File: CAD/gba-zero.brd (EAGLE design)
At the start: 15.2 x 11.4 mm, 20 parts, among them IC5 APX803, Q2 BSS138

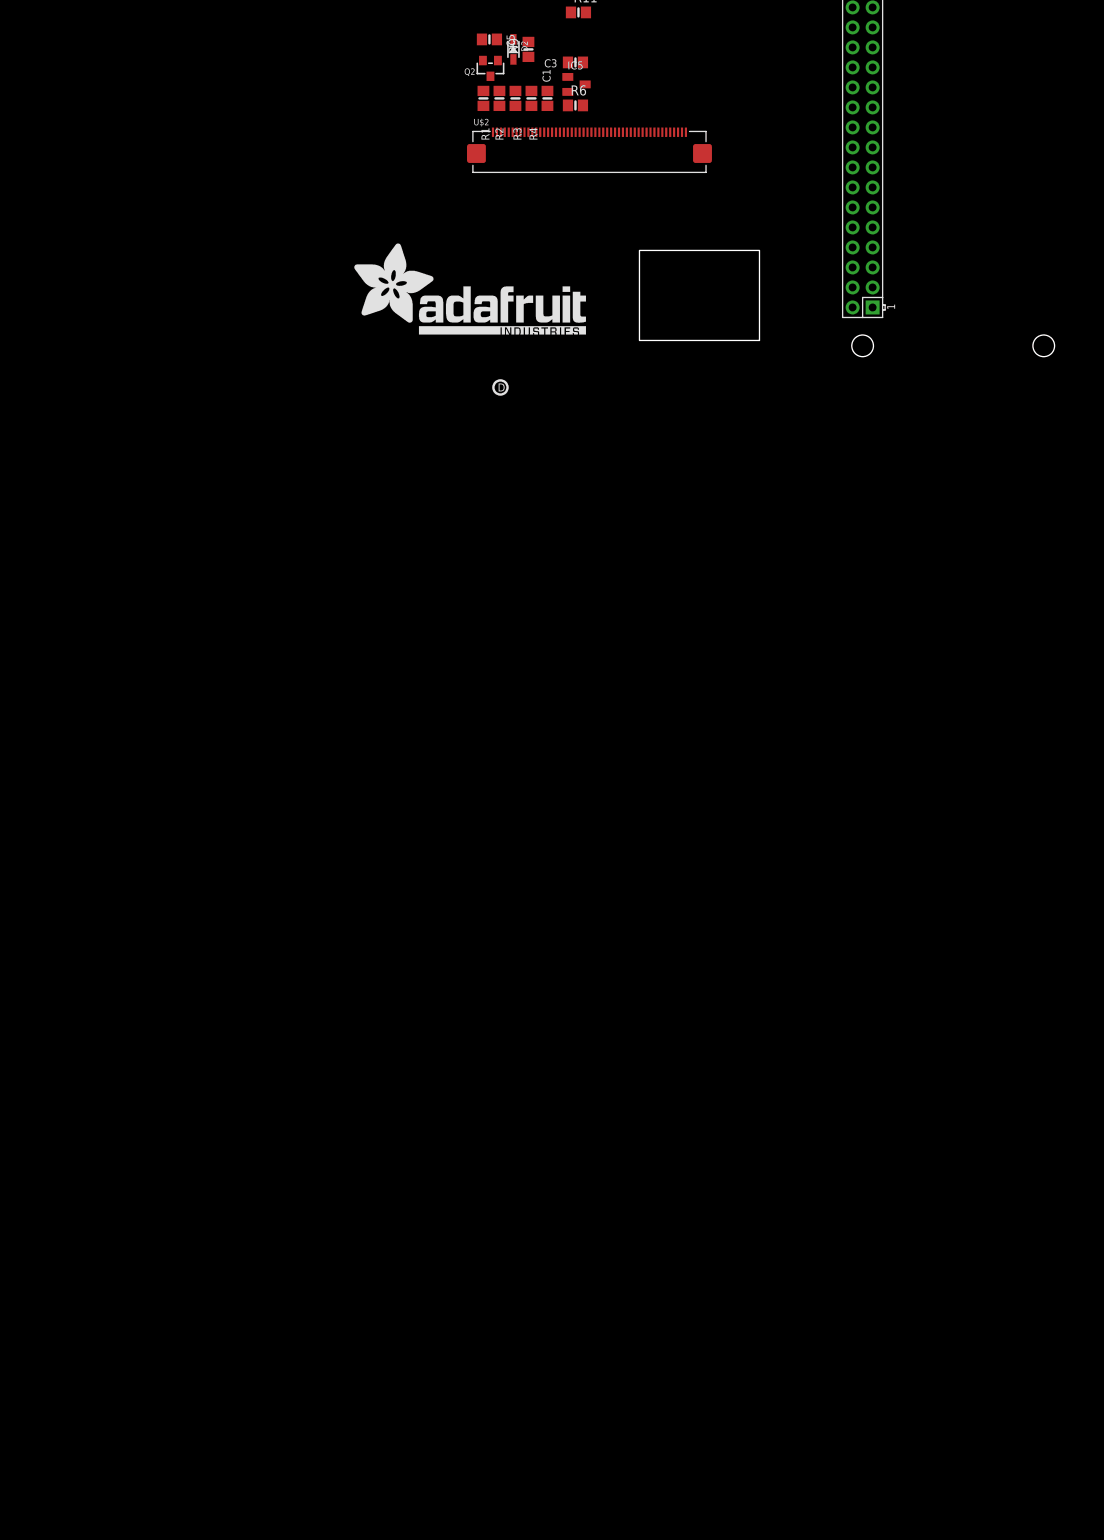
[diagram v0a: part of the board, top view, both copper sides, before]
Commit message: Parts & Schematic almost done, except AB buttons
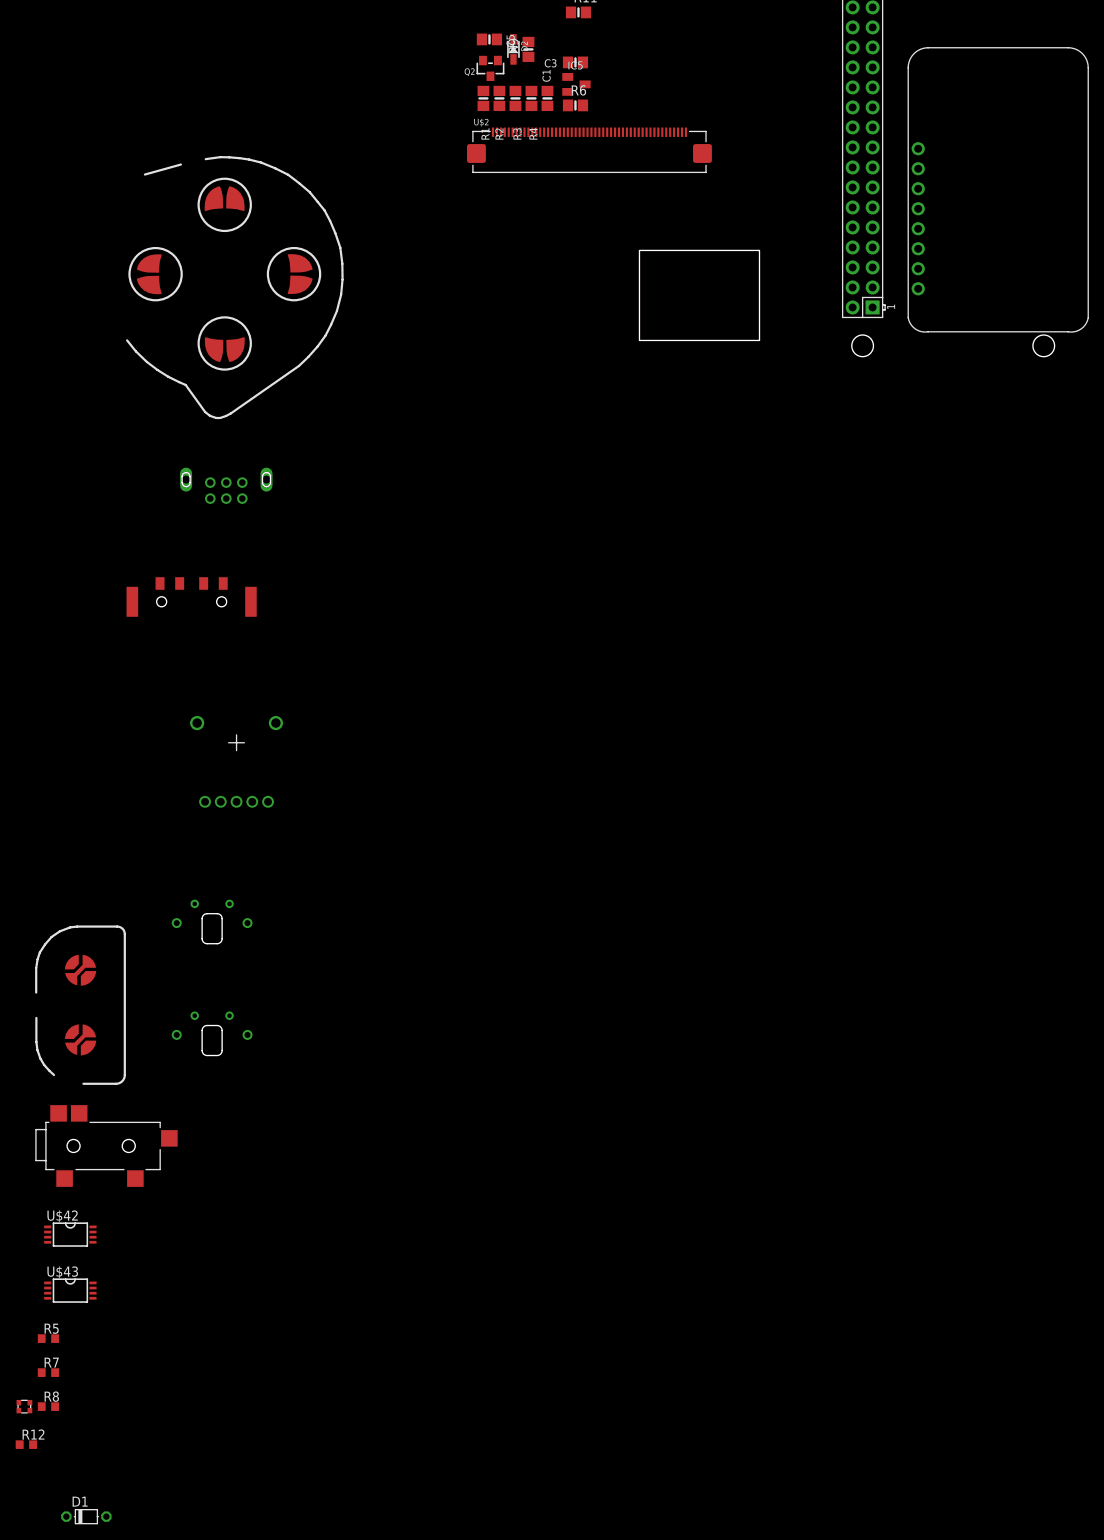
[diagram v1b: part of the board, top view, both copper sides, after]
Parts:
- removed U$23: (no value), microbuilder:ADAFRUIT_TEXT_20MM
- added D1: (no value), diode:D-5
- added R12: 10KΩ, resistor:R0603
- added R5, R7: 250Ω, resistor:R0603
- added R8: 167Ω, resistor:R0603
- added U$10: LINK_CONNECTOR, gba-zero-parts:LINK_CONNECTOR
- added U$11: PWR_SWITCH, gba-zero-parts:PWR-SWITCH
- added U$15: RK10J12E0A0A, gba-zero-parts:RK10J12E0A0A
- added U$16, U$17: SHOULDER_BUTTON, gba-zero-parts:SHOULDER_BUTTON
- added U$18: START_SELECT_BUTTON, gba-zero-parts:START_SELECT_BUTTON
- added U$22: SWTCHCRFT_3.5JACK5-JACK-SMD, gba-zero-parts:4-JACK-SMD
- added U$3: D-PAD, gba-zero-parts:D-PAD
- added U$43: 74LVC3G04, gba-zero-parts:TSSOP-8
- added U$44: LTST-C19HE1WT, gba-zero-parts:WL-SBCW-0606
- U$12: value (none) -> POWERBOOST-1000C; device microbuilder:PCBFEAT-REV-040 -> gba-zero-parts:POWERBOOST-1000C
- U$2: value DISP_LCD_240X320_50PIN_2.8IN -> (none); device microbuilder:TFT_2.83IN_240X320_50PIN -> gba-zero-parts:TFT_2.83IN_240X320_50PIN
- U$42: value (none) -> 74LVC2G02; device microbuilder:ADAFRUIT_TEXT_30MM -> gba-zero-parts:TSSOP-8
- moved U$42 119.8 mm to (-34.8, -105.2)
- moved U$12 67.4 mm to (71.6, 45.5), turned to 270 degrees
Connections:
- new net GPIO17: U$17.BIG-1, U$17.SMALL-1, U$7.11
- new net GPIO19: U$18.SEL, U$7.35
- new net GPIO20: U$11.L, U$7.38
- new net GPIO21: D1.A, U$7.40
- new net GPIO22: U$3.RIGHT, U$7.15
- new net GPIO26: U$18.STR, U$7.37
- new net GPIO27: U$3.LEFT, U$7.13
- new net GPIO4: U$16.BIG-1, U$16.SMALL-1, U$7.7
- new net GPIO5: U$3.UP, U$7.29
- new net GPIO6: U$3.DOWN, U$7.31
- new net LBO: U$12.LBO, U$42.6
- new net N$11: R8.1, U$43.2
- new net N$12: R5.2, U$44.B
- new net N$13: R7.2, U$44.G
- new net N$14: R8.2, U$44.R
- new net N$15: U$42.7, U$43.1
- new net N$16: U$42.1, U$42.3, U$43.6
- new net N$17: R12.1, U$11.R
- new net N$18: D1.C, R12.2, U$12.EN
- new net N$5: R5.1, U$43.7
- new net N$8: R7.1, U$43.5
- new net USB: U$10.1, U$10.2, U$10.3, U$12.USB, U$42.2, U$42.5, U$43.3
- net +5V: now also U$12.5V, U$42.8, U$43.8, U$44.VCC
- net GND: now also U$10.4, U$10.5, U$10.6, U$10.GND@1, U$10.GND@2, U$11.C@1, U$11.C@2, U$11.GND@1, U$11.GND@2, U$12.GND@1, U$12.GND@2, U$16.BIG-2, U$16.SMALL-2, U$17.BIG-2, U$17.SMALL-2, U$18.GND@1, U$18.GND@2, U$18.GND@3, U$18.GND@4, U$3.GND@1, U$3.GND@2, U$3.GND@3, U$3.GND@4, U$42.4, U$43.4
- net RT_INT: now also U$2.44; no longer U$2.46
- net SCL: now also U$2.45; no longer U$2.44
- net SDA: now also U$2.47; no longer U$2.45

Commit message: Added AB_BUTTON part to library & schematic
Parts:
- added U$20: AB_BUTTON, gba-zero-parts:AB_BUTTON
- moved U$3 106.5 mm to (90.7, 28.0)
- moved U$12 33.4 mm to (59.4, 76.7), turned to 0 degrees
- renumbered U$16 to L, U$17 to R
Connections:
- new net 5.0V: C5.1, R1.1, R2.1, R3.1, R4.1, U$12.5V, U$42.8, U$43.8, U$44.VCC
- new net GPIO12: U$20.B@1, U$20.B@2, U$7.32
- new net GPIO23: U$20.A@1, U$20.A@2, U$7.16
- net +5V: no longer C5.1, R1.1, R2.1, R3.1, R4.1, U$12.5V, U$42.8, U$43.8, U$44.VCC
- net GND: now also U$20.GND@1, U$20.GND@2, U$20.GND@3, U$20.GND@4
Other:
- board size 15.2 x 11.4 mm -> 100 x 80 mm

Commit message: Added audio to schematic
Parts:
- removed U$15: RK10J12E0A0A, gba-zero-parts:RK10J12E0A0A
- removed U$22: SWTCHCRFT_3.5JACK5-JACK-SMD, gba-zero-parts:4-JACK-SMD
- added C12, C13, C15, C18: 10u, rcl:C0805
- added C17: 100n, rcl:C0805
- added C2, C8: 0.1μF, rcl:C0603
- added C4: 100μF, rcl:C0603
- added C6: 47μF, rcl:C0603
- added R13: 150Ω, resistor:R0603
- added R14: 220Ω, resistor:R0603
- added R15, R19: 100KΩ, resistor:R0603
- added R16: 100Ω, resistor:R0603
- added R17, R20: 0Ω, resistor:R0603
- added R18: 1.8KΩ, resistor:R0603
- added SP1: SPEAKER, GBA:SPEAKER
- added U$16: SWTCHCRFT_3.5JACK5-JACK-SMD, gba-zero-parts:4-JACK-SMD
- added U$17: 10K, gba-zero-parts:RK10J12E0A0A
- added U1: NC7WZ16, fairchild:SC-70-6
- added U4: LM4875, texas:SOIC8
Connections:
- new net GPIO13: U$7.33, U1.1
- new net N$19: C4.2, R13.2, U$16.2, U$16.3
- new net N$20: R14.1, U1.6
- new net N$21: C2.2, C6.2, R14.2, R16.2
- new net N$22: R15.1, R19.1, U$16.5
- new net N$23: R19.2, U4.3
- new net N$24: R17.1, U$17.2O
- new net N$25: R20.1, U$17.2
- new net N$26: R17.2, R20.2, U4.4
- new net N$30: C6.1, R18.2, U4.2
- new net N$35: C12.1, U4.7
- new net N$36: C4.1, SP1.1, U4.5
- new net N$37: SP1.2, U4.8
- net +5V: now also C13.2, C15.1, C17.1, C18.1, R15.2, U$17.1, U4.1
- net 3.3V: now also C8.2, U1.5
- net GND: now also C12.2, C13.1, C15.2, C17.2, C18.2, C2.1, C8.1, R13.1, R16.1, R18.1, U$16.1, U$17.3, U$17.3O, U1.2, U4.6

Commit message: Lots of schematic cleanup
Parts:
- removed R13: 150Ω, resistor:R0603
- removed R14: 220Ω, resistor:R0603
- removed R15, R19: 100KΩ, resistor:R0603
- removed R16: 100Ω, resistor:R0603
- removed R18: 1.8KΩ, resistor:R0603
- added R21: 250, microbuilder:0805
- added R22, R23: 100K, microbuilder:0805
- added R24: 150, microbuilder:0805
- added WPJ4: 0, microbuilder:SOLDERJUMPER_CLOSEDWIRE
- C1, C3, C5, R1, R10, R11, R2, R3, R4, R6, R9: device microbuilder:0805-NO -> microbuilder:0805
- D1: value (none) -> IN4001
- R12: value 10KΩ -> 1.8K; device resistor:R0603 -> microbuilder:0805
- R17: value 0Ω -> 167; device resistor:R0603 -> microbuilder:0805
- R20: value 0Ω -> 250; device resistor:R0603 -> microbuilder:0805
- R5: value 250Ω -> 10K; device resistor:R0603 -> microbuilder:0805
- R7: value 250Ω -> 220; device resistor:R0603 -> microbuilder:0805
- R8: value 167Ω -> 100; device resistor:R0603 -> microbuilder:0805
- U$2: value (none) -> 50_PIN_CON
- U$7: device RPI-Zero:RASPBERRYPI_BASTELSTUBE_V13_RASPI_BOARD_B+_FULL -> gba-zero-parts:RASPBERRYPI_BASTELSTUBE_V13_RASPI_BOARD_B+_FULL
- WPJ1: value (none) -> 0
- moved R5 200.9 mm to (-40.1, -319.3)
- moved R7 199.2 mm to (-40.1, -321.8)
- moved R8 197.4 mm to (-40.1, -324.4)
- moved R12 195.1 mm to (-40.1, -326.9)
- moved R17 19.3 mm to (-40.1, -311.7)
- moved R20 17.0 mm to (-40.1, -314.2)
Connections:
- net GPIO12 renamed BTN_B
- net GPIO13 renamed AUD_PWM
- net GPIO17 renamed BTN_RS
- net GPIO18 renamed BKLT_PWM
- net GPIO19 renamed BTN_SEL
- net GPIO20 renamed PWR_SW_SEN
- net GPIO21 renamed PWR_EN_RPI
- net GPIO22 renamed BTN_R
- net GPIO23 renamed BTN_A
- net GPIO26 renamed BTN_STR
- net GPIO27 renamed BTN_L
- net GPIO4 renamed BTN_LS
- net GPIO5 renamed BTN_U
- net GPIO6 renamed BTN_D
- removed net 5.0V: C5.1, R1.1, R2.1, R3.1, R4.1, U$12.5V, U$42.8, U$43.8, U$44.VCC
- removed net N$19: C4.2, R13.2, U$16.2, U$16.3
- removed net N$24: R17.1, U$17.2O
- removed net N$25: R20.1, U$17.2
- new net BKLT: U$7.36, WPJ4.1
- new net RING: C4.2, R24.2, U$16.2, U$16.3
- new net RXD: U$10.3, U$7.10
- new net TXD: U$10.4, U$7.8
- net +5V: now also C5.1, R1.1, R2.1, R23.1, R3.1, R4.1, U$12.5V, U$42.8, U$43.8, U$44.VCC; no longer R15.2
- net GND: now also R12.2, R24.1, R8.2; no longer R13.1, R16.1, R18.1, U$10.4
- net N$11: now also R20.2, U$43.5; no longer R8.1, U$43.2
- net N$12: now also R20.1, U$44.G; no longer R5.2, U$44.B
- net N$13: now also R21.2, U$43.7; no longer R7.2, U$44.G
- net N$14: now also R21.1, U$44.B; no longer R8.2, U$44.R
- net N$17: now also R5.2; no longer R12.1
- net N$18: now also R5.1; no longer R12.2
- net N$20: now also R7.2; no longer R14.1
- net N$21: now also R7.1, R8.1; no longer R14.2, R16.2
- net N$22: now also R22.2, R23.2; no longer R15.1, R19.1
- net N$23: now also R22.1; no longer R19.2
- net N$26: now also U$17.2; no longer R17.2, R20.2
- net N$30: now also R12.1; no longer R18.2
- net N$5: now also R17.2, U$43.2; no longer R5.1, U$43.7
- net N$6: now also WPJ4.2
- net N$8: now also R17.1, U$44.R; no longer R7.1, U$43.5
- net USB: no longer U$10.3

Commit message: Added JST battery connector
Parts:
- added CN1: (no value), gba-zero-parts:JSTPH2
- moved U$12 93.5 mm to (62.7, -16.8)
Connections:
- new net N$19: CN1.BAT, U$12.BAT
- net GND: now also CN1.GND
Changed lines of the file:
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@@
 <element name="R" library="gba-zero-parts" package="SHOULDER_BUTTON" value="SHOULDER_BUTTON" x="-16.8" y="-79.8"/>
 <element name="U$18" library="gba-zero-parts" package="START_SELECT_BUTTON" value="START_SELECT_BUTTON" x="-33.5" y="-76"/>
-<element name="U$12" library="gba-zero-parts" package="POWERBOOST-1000C" value="POWERBOOST-1000C" x="59.352" y="76.668"/>
+<element name="U$12" library="gba-zero-parts" package="POWERBOOST-1000C" value="POWERBOOST-1000C" x="62.654" y="-16.804"/>
 <element name="U$42" library="gba-zero-parts" package="TSSOP-8" value="74LVC2G02" x="-34.798" y="-105.156"/>
 <element name="U$43" library="gba-zero-parts" package="TSSOP-8" value="74LVC3G04" x="-34.798" y="-112.268"/>
@@
 <element name="R23" library="microbuilder" package="0805" value="100K" x="-40.132" y="-331.978"/>
 <element name="R24" library="microbuilder" package="0805" value="150" x="-40.132" y="-334.518"/>
+<element name="CN1" library="gba-zero-parts" package="JSTPH2" value="" x="-8.89" y="-319.278"/>
 </elements>
 <signals>
@@
 <contactref element="U$2" pad="49"/>
 <contactref element="U$2" pad="48"/>
+<contactref element="CN1" pad="GND"/>
 <wire x1="-23.202" y1="-216.662" x2="-34.886" y2="-216.662" width="0" layer="19" extent="1-1"/>
 <wire x1="-7.962" y1="-221.996" x2="-23.202" y2="-216.662" width="0" layer="19" extent="1-1"/>
@@
 <wire x1="100.0525" y1="26.706" x2="91.988" y2="37.3105" width="0" layer="19" extent="1-1"/>
 <wire x1="89.448" y1="18.6415" x2="81.3835" y2="29.246" width="0" layer="19" extent="1-1"/>
-<wire x1="82.339" y1="77.938" x2="67.07" y2="60.83" width="0" layer="19" extent="1-1"/>
-<wire x1="87.419" y1="77.938" x2="82.339" y2="77.938" width="0" layer="19" extent="1-1"/>
+<wire x1="85.641" y1="-15.534" x2="67.07" y2="60.83" width="0" layer="19" extent="1-1"/>
+<wire x1="90.721" y1="-15.534" x2="85.641" y2="-15.534" width="0" layer="19" extent="1-1"/>
 <wire x1="-39.182" y1="-324.358" x2="-38.928" y2="-262.636" width="0" layer="19" extent="1-1"/>
 <wire x1="-39.182" y1="-326.898" x2="-39.182" y2="-324.358" width="0" layer="19" extent="1-1"/>
 <wire x1="-41.082" y1="-334.518" x2="-39.182" y2="-326.898" width="0" layer="19" extent="1-1"/>
+<wire x1="-9.89" y1="-322.978" x2="-41.082" y2="-334.518" width="0" layer="19" extent="1-1"/>
 </signal>
 <signal name="MISO">
@@
 <wire x1="-17.032" y1="-11.7" x2="-37.673" y2="-104.831" width="0" layer="19" extent="1-1"/>
 <wire x1="-17.032" y1="-9.668" x2="-17.032" y2="-11.7" width="0" layer="19" extent="1-1"/>
-<wire x1="72.179" y1="77.938" x2="-17.032" y2="-9.668" width="0" layer="19" extent="1-1"/>
+<wire x1="75.481" y1="-15.534" x2="-17.032" y2="-9.668" width="0" layer="19" extent="1-1"/>
 </signal>
 <signal name="N$16">
@@
 <contactref element="U$42" pad="6"/>
 <contactref element="U$12" pad="LBO"/>
-<wire x1="84.879" y1="77.938" x2="-31.923" y2="-105.481" width="0" layer="19" extent="1-1"/>
+<wire x1="88.181" y1="-15.534" x2="-31.923" y2="-105.481" width="0" layer="19" extent="1-1"/>
 </signal>
 <signal name="N$18">
@@
 <contactref element="R5" pad="1"/>
 <wire x1="-41.082" y1="-319.278" x2="-35.306" y2="-140.97" width="0" layer="19" extent="1-1"/>
-<wire x1="79.799" y1="77.938" x2="-35.306" y2="-140.97" width="0" layer="19" extent="1-1"/>
+<wire x1="83.101" y1="-15.534" x2="-35.306" y2="-140.97" width="0" layer="19" extent="1-1"/>
 </signal>
 <signal name="PWR_EN_RPI">
@@
 <wire x1="17.653" y1="40.066" x2="19.685" y2="40.066" width="0" layer="19" extent="1-1"/>
 <wire x1="17.465" y1="46.609" x2="17.653" y2="40.066" width="0" layer="19" extent="1-1"/>
-<wire x1="89.959" y1="77.938" x2="64.53" y2="15.11" width="0" layer="19" extent="1-1"/>
+<wire x1="93.261" y1="-15.534" x2="64.53" y2="15.11" width="0" layer="19" extent="1-1"/>
 </signal>
 <signal name="N$21">
@@
 <wire x1="-41.082" y1="-316.738" x2="-39.94" y2="-127.5" width="0" layer="19" extent="1-1"/>
 </signal>
+<signal name="N$19">
+<contactref element="U$12" pad="BAT"/>
+<contactref element="CN1" pad="BAT"/>
+<wire x1="-7.89" y1="-322.978" x2="78.021" y2="-15.534" width="0" layer="19" extent="1-1"/>
+</signal>
 </signals>

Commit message: Added new parts for SMD RPI, just the 510 pin FPC connector Sorted parts in the layout
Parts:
- U$2: device gba-zero-parts:TFT_2.83IN_240X320_50PIN -> gba-zero-parts:FPC-50-CON
- U$7: value RPI-ZERO -> RPI-ZEROSMD; device gba-zero-parts:RASPBERRYPI_BASTELSTUBE_V13_RASPI_BOARD_B+_FULL -> gba-zero-parts:RPI-SMD
- moved R20 432.1 mm to (112.8, 89.9)
- moved R21 432.0 mm to (112.5, 87.4)
- moved R17 424.6 mm to (112.5, 84.6)
- moved CN1 407.8 mm to (47.8, 84.6)
- moved R24 402.2 mm to (180.8, 1.52)
- moved R23 401.8 mm to (180.8, 3.56)
- moved R22 401.3 mm to (180.8, 5.59)
- moved R12 387.7 mm to (154.2, 8.64), turned to 270 degrees
- moved R8 382.9 mm to (148.8, 8.64), turned to 90 degrees
- moved R7 378.6 mm to (144.3, 8.89), turned to 90 degrees
- moved C4 347.3 mm to (180.8, -0.51), turned to 180 degrees
- moved C13 345.1 mm to (161.3, 20.8)
- moved WPJ4 341.4 mm to (68.3, 14.5), turned to 90 degrees
- moved C15 339.7 mm to (137.4, 32.3)
- moved C18 339.7 mm to (137.2, 34.8)
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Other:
- board size 100 x 80 mm -> 133.3 x 73.7 mm

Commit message: Added Ryzee's parts for placement
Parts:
- added D3: DUAL_LED, GBA:DUAL_LED
- added R13: 27k, GBA:VOLUME
- added SW1: LEFT, GBA:BUMPER
- added SW2: RIGHT, GBA:BUMPER
- added SW3: PWR_SWITCH, GBA:PWR_SWITCH
- added X1: LINK_SOCKET, GBA:LINK_SOCKET
- added X2: HEADPHONE, GBA:HEADPHONE
- moved U$20 175.9 mm to (290.3, 55.4)
- moved C12 172.4 mm to (329.7, 6.60)
- moved C13 172.4 mm to (333.5, 28.4)
- moved C18 172.4 mm to (309.4, 42.4)
- moved C3 172.4 mm to (209.2, 89.7)
- moved C5 172.4 mm to (209.2, 92.3)
- moved C6 172.4 mm to (323.6, 16.5)
- moved R 172.4 mm to (300.4, 75.9)
- moved R1 172.4 mm to (227.3, 22.5)
- moved R2 172.4 mm to (227.3, 24.8)
- moved R3 172.4 mm to (227.3, 27.1)
- moved R4 172.4 mm to (227.3, 29.3)
- moved R5 172.4 mm to (166.1, 11.4)
- moved R6 172.4 mm to (227.3, 33.9)
- moved R9 172.4 mm to (227.3, 31.6)
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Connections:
- net GND: now also X2.GND
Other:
- board size 133.3 x 73.7 mm -> 284.3 x 74.3 mm

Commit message: Started the layout. Tweaking parts as necessary
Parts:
- removed D3: DUAL_LED, GBA:DUAL_LED
- removed R13: 27k, GBA:VOLUME
- removed SW1: LEFT, GBA:BUMPER
- removed SW2: RIGHT, GBA:BUMPER
- removed SW3: PWR_SWITCH, GBA:PWR_SWITCH
- removed X1: LINK_SOCKET, GBA:LINK_SOCKET
- removed X2: HEADPHONE, GBA:HEADPHONE
- moved U$2 246.5 mm to (-27.8, 37.1)
- moved D2 238.8 mm to (0.15, 34.3)
- moved IC5 238.8 mm to (-5.56, 43.3)
- moved Q2 238.8 mm to (-4.80, 38.3)
- moved R1 238.8 mm to (-11.4, 29.0)
- moved R10 238.8 mm to (-11.1, 48.2)
- moved R11 238.8 mm to (-11.1, 45.9)
- moved R2 238.8 mm to (-11.4, 31.3)
- moved R3 238.8 mm to (-11.4, 33.6)
- moved R4 238.8 mm to (-11.4, 35.9)
- moved R6 238.8 mm to (-11.4, 40.4)
- moved R9 238.8 mm to (-11.4, 38.1)
- moved WPJ1 238.8 mm to (-1.37, 28.5)
- moved WPJ4 238.8 mm to (1.81, 28.6)
- moved C1 192.2 mm to (18.3, 110.9)
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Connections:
- net GND: no longer X2.GND
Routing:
- net +5V: track 0.00 -> 28.2 mm
- net USB: track 0.00 -> 15.1 mm
- net N$16: track 0.00 -> 14.9 mm, vias 0 -> 2
- net N$5: track 0.00 -> 13.4 mm, vias 0 -> 2
- net N$8: track 0.00 -> 8.07 mm
- net LBO: track 0.00 -> 7.52 mm
- net N$13: track 0.00 -> 6.91 mm
- net N$15: track 0.00 -> 6.81 mm
- net N$11: track 0.00 -> 5.88 mm
- net N$12: track 0.00 -> 5.72 mm
- net N$14: track 0.00 -> 5.45 mm
- added copper zone on layer 1, net GND
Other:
- board size 284.3 x 74.3 mm -> 130.7 x 72.9 mm
